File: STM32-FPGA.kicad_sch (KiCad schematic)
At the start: 18 parts, among them J1 USB4105-GF-A-120, J4 Conn_01x04, J5 Conn_01x05, U4 USBLC6-2SC6

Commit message: power supply
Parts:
- removed J4: Conn_01x04, symbol Connector_Generic:Conn_01x04
- removed J5: Conn_01x05, symbol Connector_Generic:Conn_01x05
- removed R10, R12, R18, R19, R20, R21: 0R, symbol Device:R_US
- removed R11, R13, R22, R23, R24, R25: 33R, symbol Device:R_US
- removed U4: USBLC6-2SC6, Package_TO_SOT_SMD:SOT-23-6, symbol Power_Protection:USBLC6-2SC6
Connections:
- net ESD_D+ renamed PRUSB_D+
- net ESD_D- renamed PRUSB_D-
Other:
- removed sheet 10M08SAU324C8G
- removed sheet Programmer
- removed sheet STM32F103C8T6
- note removed: "must look into power multiple buck converters maybe required???"
- moved on the sheet: J1, R8, R9

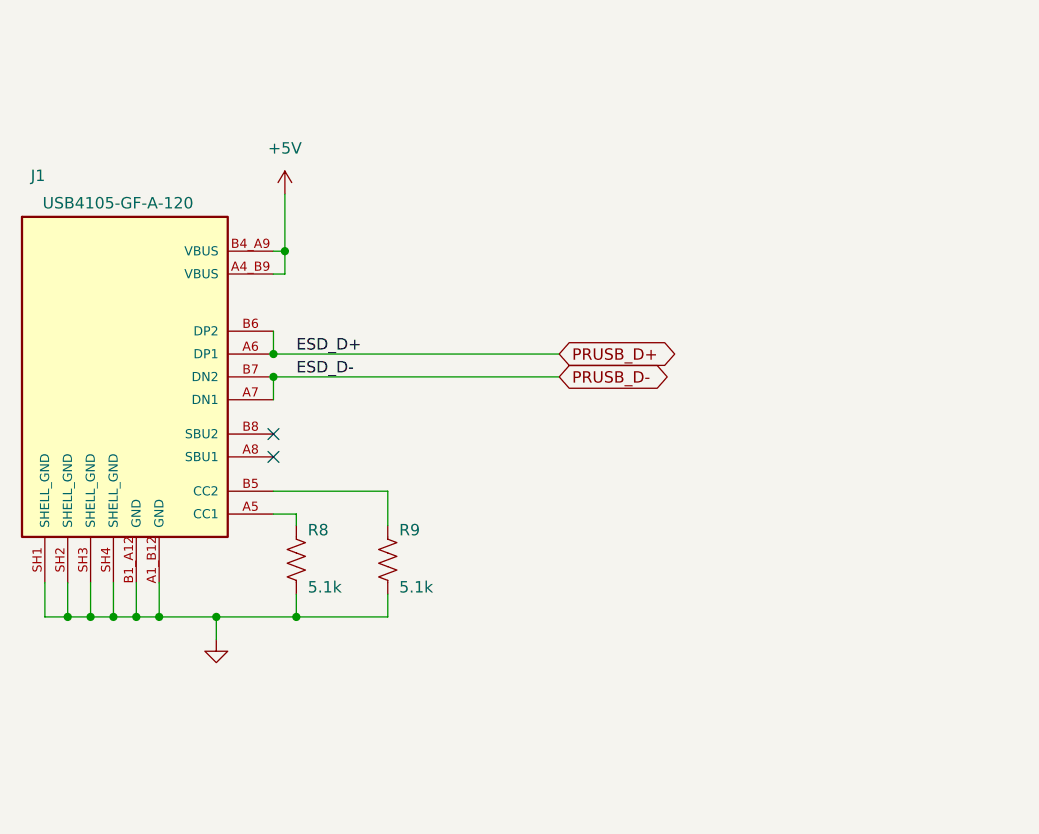
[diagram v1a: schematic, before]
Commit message: CL1025YU258 symbol created
The schematic symbol for the CL1025YU258 was created. A block diagram representing the architecture of the board has been added to the root page.
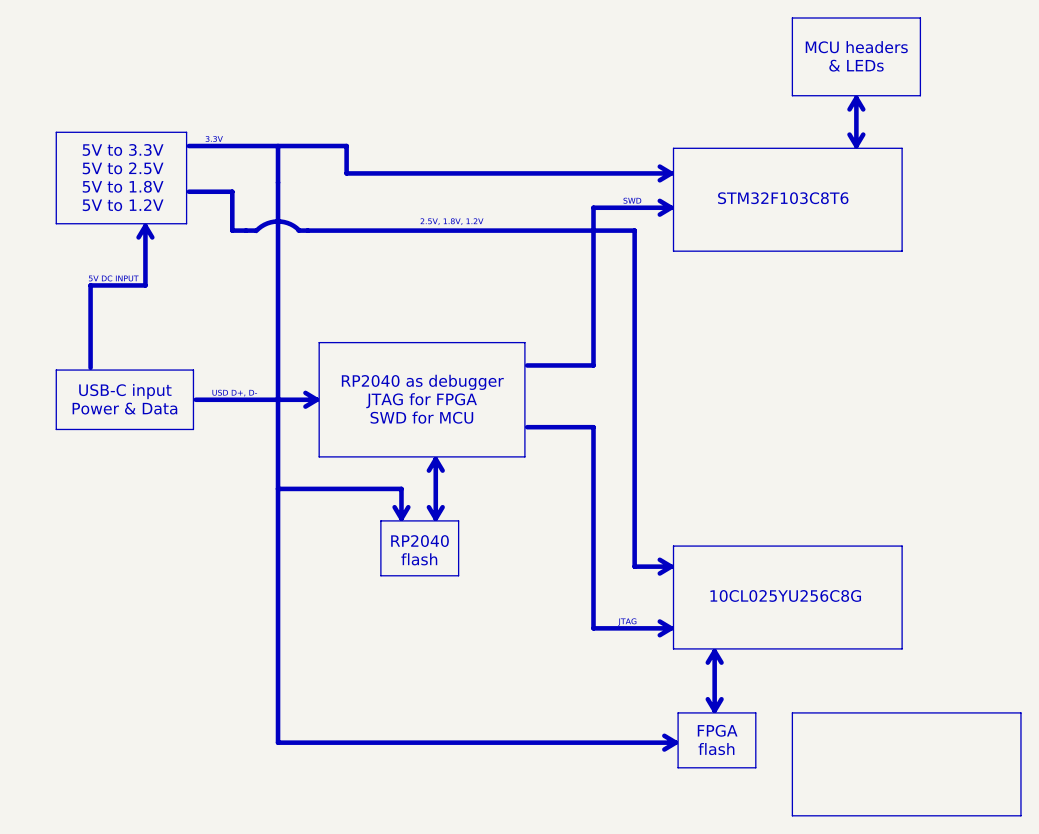
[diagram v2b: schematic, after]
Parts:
- removed J1: USB4105-GF-A-120, USB4105-GF-A-120:GCT_USB4105-GF-A-120, symbol USB4105-GF-A-120:USB4105-GF-A-120
- removed R8, R9: 5.1k, symbol Device:R_US
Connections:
- no-connect marks 2 -> 0
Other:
- note added: "10CL025YU256C8G"
- note added: "2.5V, 1.8V, 1.2V"
- note added: "3.3V"
- note added: "5V DC INPUT"
- note added: "5V to 3.3V 5V to 2.5V 5V to 1.8V 5V to 1.2V"
- note added: "FPGA flash"
- note added: "JTAG"
- note added: "MCU headers & LEDs"
- note added: "RP2040 as debugger JTAG for FPGA SWD for MCU"
- note added: "RP2040 flash"
- note added: "STM32F103C8T6"
- note added: "SWD"
- note added: "USB-C input Power & Data"
- note added: "USD D+, D-"

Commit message: No big changes made from last time
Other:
- note added: "3.3V, 2.5V, 1.8V, 1.2V"
- note removed: "2.5V, 1.8V, 1.2V"
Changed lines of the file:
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@@
 		)
 	)
-	(text "2.5V, 1.8V, 1.2V"
+	(text "3.3V, 2.5V, 1.8V, 1.2V"
 		(exclude_from_sim no)
 		(at 93.472 71.882 0)
